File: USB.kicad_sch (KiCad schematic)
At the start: 52 parts, among them J2 Conn_02x05_Odd_Even, J3 USB_A_Stacked, J4 USB_A_Stacked, U1 IMX6UL, U10 FE2.1, U8 X1000, Y1 12MHz

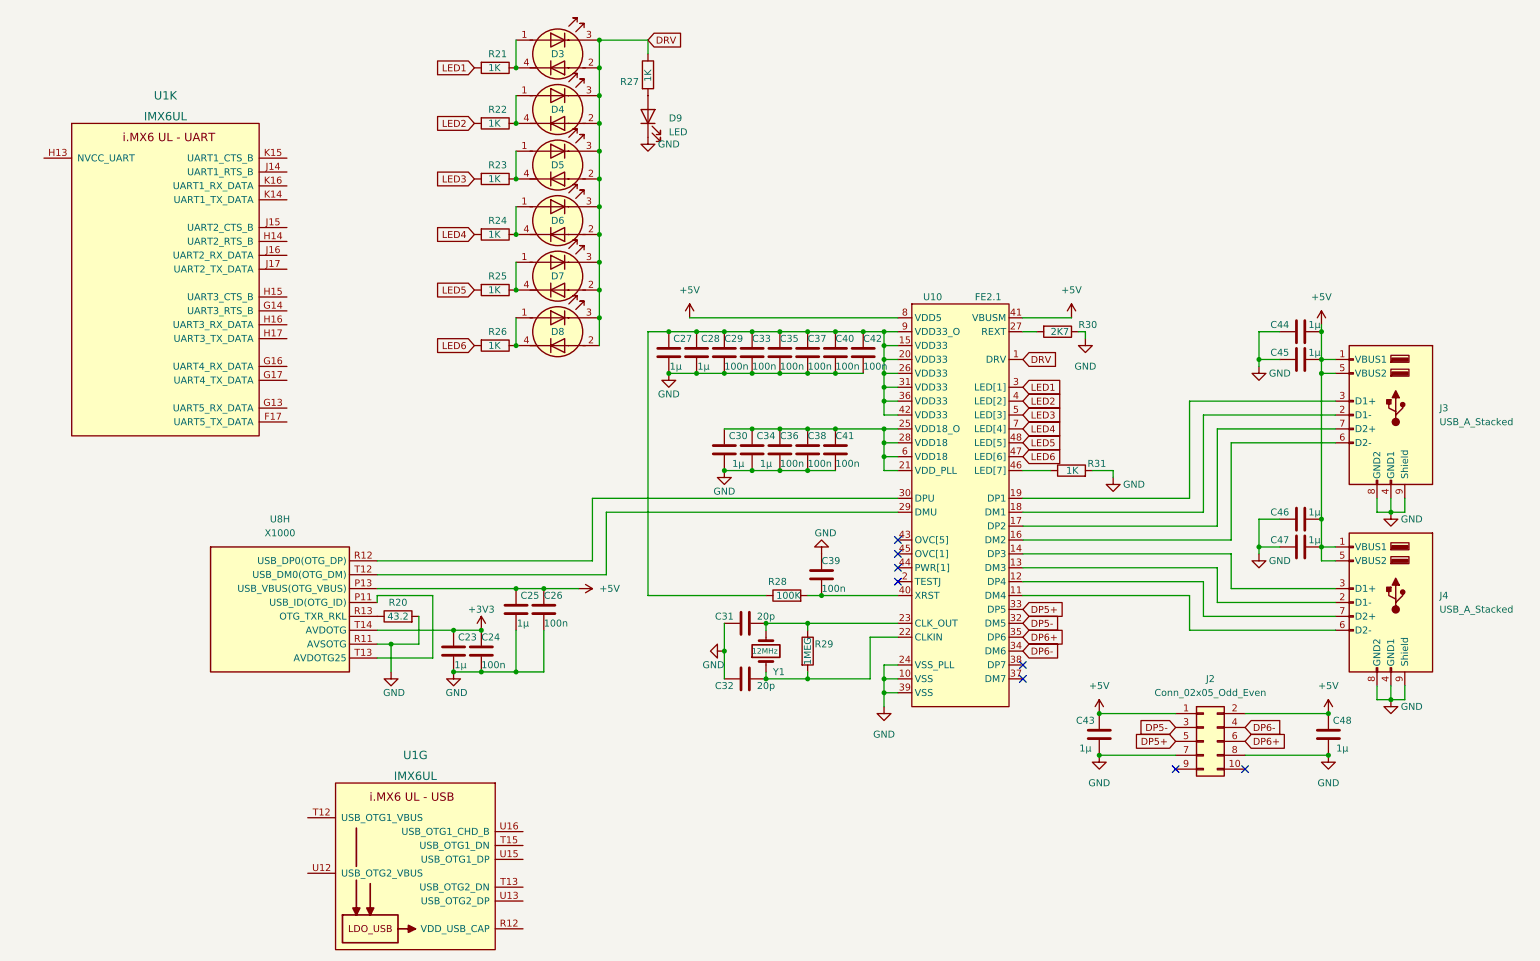
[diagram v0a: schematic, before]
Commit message: Display Update
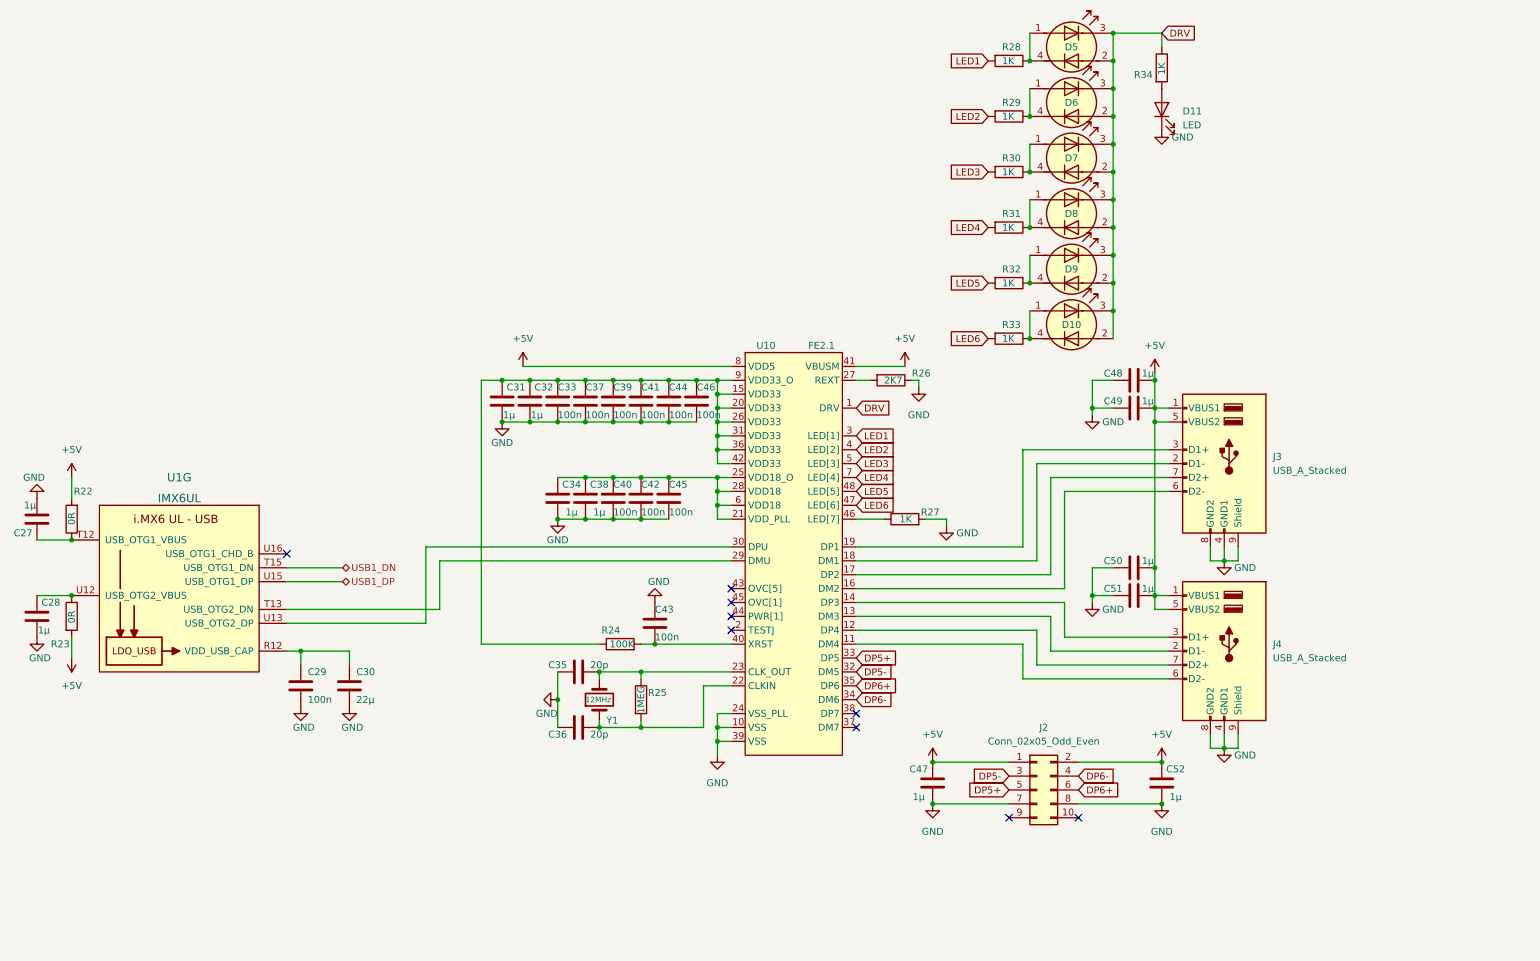
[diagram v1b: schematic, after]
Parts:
- removed C23, C25: 1µ, Capacitor_SMD:C_0402_1005Metric, symbol Device:C
- removed C24, C26: 100n, Capacitor_SMD:C_0402_1005Metric, symbol Device:C
- removed R20: 43.2, Resistor_SMD:R_0402_1005Metric, symbol Device:R
- removed unit 11 of U1
- removed U8: X1000, TheBrutzlers_Lib:BGA256C80P16X16_1300X1300X130N, symbol TheBrutzlers_Lib:X1000
- added C27, C28: 1µ, Capacitor_SMD:C_0402_1005Metric, symbol Device:C
- added C29: 100n, Capacitor_SMD:C_0402_1005Metric, symbol Device:C
- added C30: 22µ, Capacitor_SMD:C_0603_1608Metric, symbol Device:C
- added R22, R23: 0R, Resistor_SMD:R_0402_1005Metric, symbol Device:R
- renumbered C27 to C31, C28 to C32, C29 to C33, C30 to C34, C31 to C35, C32 to C36, C33 to C37, C34 to C38, C35 to C39, C36 to C40, C37 to C41, C38 to C42, C39 to C43, C40 to C44, C41 to C45, C42 to C46, C43 to C47, C44 to C48, C45 to C49, C46 to C50, C47 to C51, C48 to C52, D8 to D10, D9 to D11, D3 to D5, D4 to D6, D5 to D7, D6 to D8, D7 to D9, R28 to R24, R29 to R25, R30 to R26, R31 to R27, R21 to R28, R22 to R29, R23 to R30, R24 to R31, R25 to R32, R26 to R33, R27 to R34
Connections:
- net +5V: now also R22.2, R23.2
- net GND: now also C27.2, C28.2, C29.2, C30.2
- net at U1.R12 (VDD_USB_CAP): now also C29.1, C30.1
- net at U1.T12 (USB_OTG1_VBUS): now also C27.1, R22.1
- net at U1.T13 (USB_OTG2_DN): now also U10.29 (DMU)
- net USB1_DN: now reaches U1.T15 (USB_OTG1_DN)
- net at U1.U12 (USB_OTG2_VBUS): now also C28.1, R23.1
- net at U1.U13 (USB_OTG2_DP): now also U10.30 (DPU)
- net USB1_DP: now reaches U1.U15 (USB_OTG1_DP)
- no-connect marks 8 -> 9
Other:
- moved on the sheet: C31, C32, C33, C34, C35, C36, C37, C38, C39, C40, C41, C42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

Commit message: update DDR
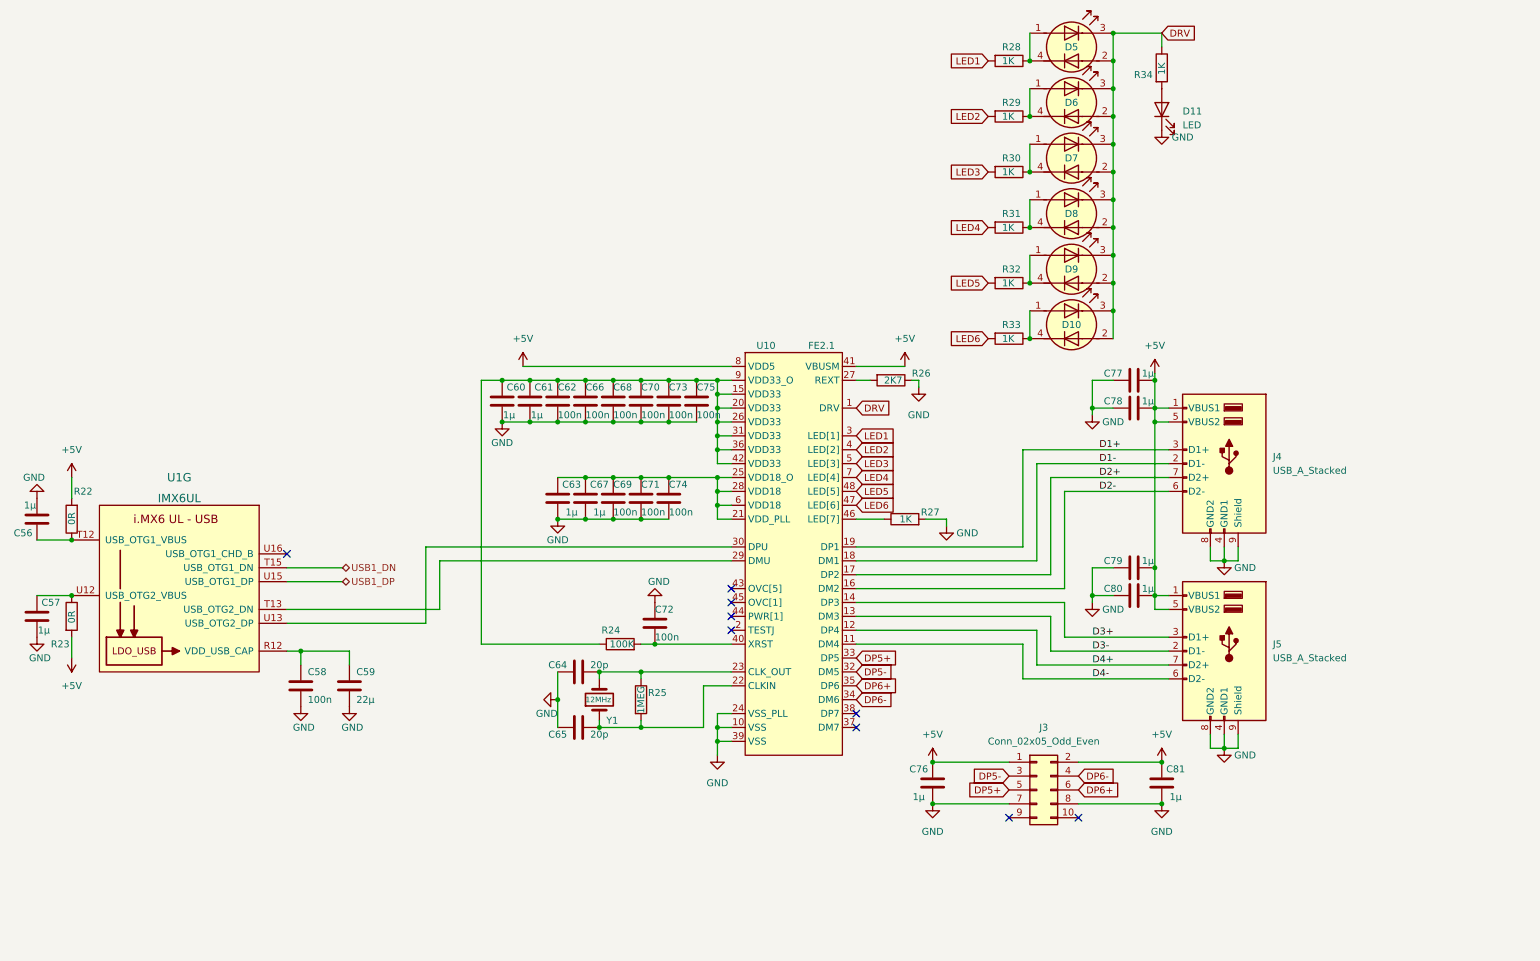
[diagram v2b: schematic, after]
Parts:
- renumbered C27 to C56, C28 to C57, C29 to C58, C30 to C59, C31 to C60, C32 to C61, C33 to C62, C34 to C63, C35 to C64, C36 to C65, C37 to C66, C38 to C67, C39 to C68, C40 to C69, C41 to C70, C42 to C71, C43 to C72, C44 to C73, C45 to C74, C46 to C75, C47 to C76, C48 to C77, C49 to C78, C50 to C79, C51 to C80, C52 to C81, J2 to J3, J3 to J4, J4 to J5
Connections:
- net D3-: now reaches J5.2 (D1-), U10.13 (DM3)
- net D3+: now reaches J5.3 (D1+), U10.14 (DP3)
- net D4-: now reaches J5.6 (D2-), U10.11 (DM4)
- net D4+: now reaches J5.7 (D2+), U10.12 (DP4)
- net D2-: now reaches J4.6 (D2-), U10.16 (DM2)
- net D2+: now reaches J4.7 (D2+), U10.17 (DP2)
- net D1-: now reaches J4.2 (D1-), U10.18 (DM1)
- net D1+: now reaches J4.3 (D1+), U10.19 (DP1)
